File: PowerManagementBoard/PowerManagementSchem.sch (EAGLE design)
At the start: 112 parts, among them J1 D15S24A4GV00LF, J8 182-037-213R531, J9 182-025-213R531, U1 VX7805-500, U2 PYB20-Q24-S5, U3 PYB30-Q48-S5, U4 PYB30-Q48-S12, U5 3V3REG, U6 INA4180-SPLIT, U7 INA4180-SPLIT, U8 TEENSY-4.0SILK, U9 INA4180-SPLIT

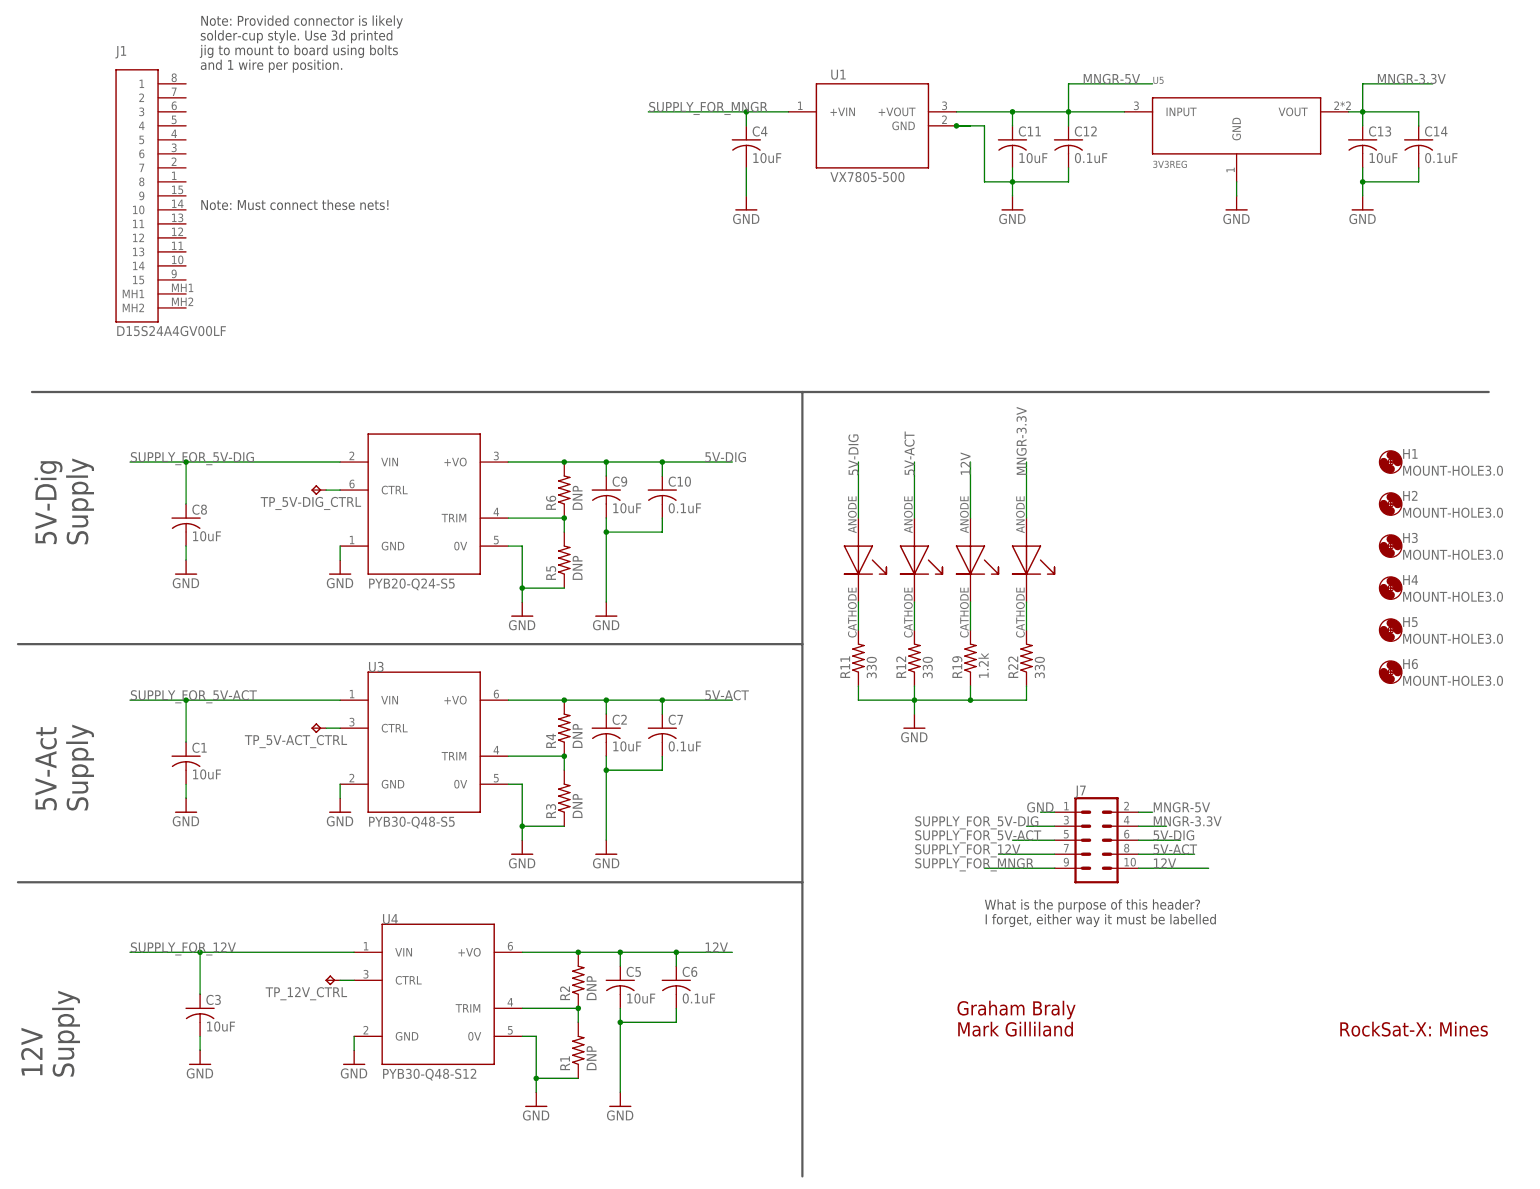
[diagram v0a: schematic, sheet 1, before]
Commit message: Moved components around on board. Updated power input header
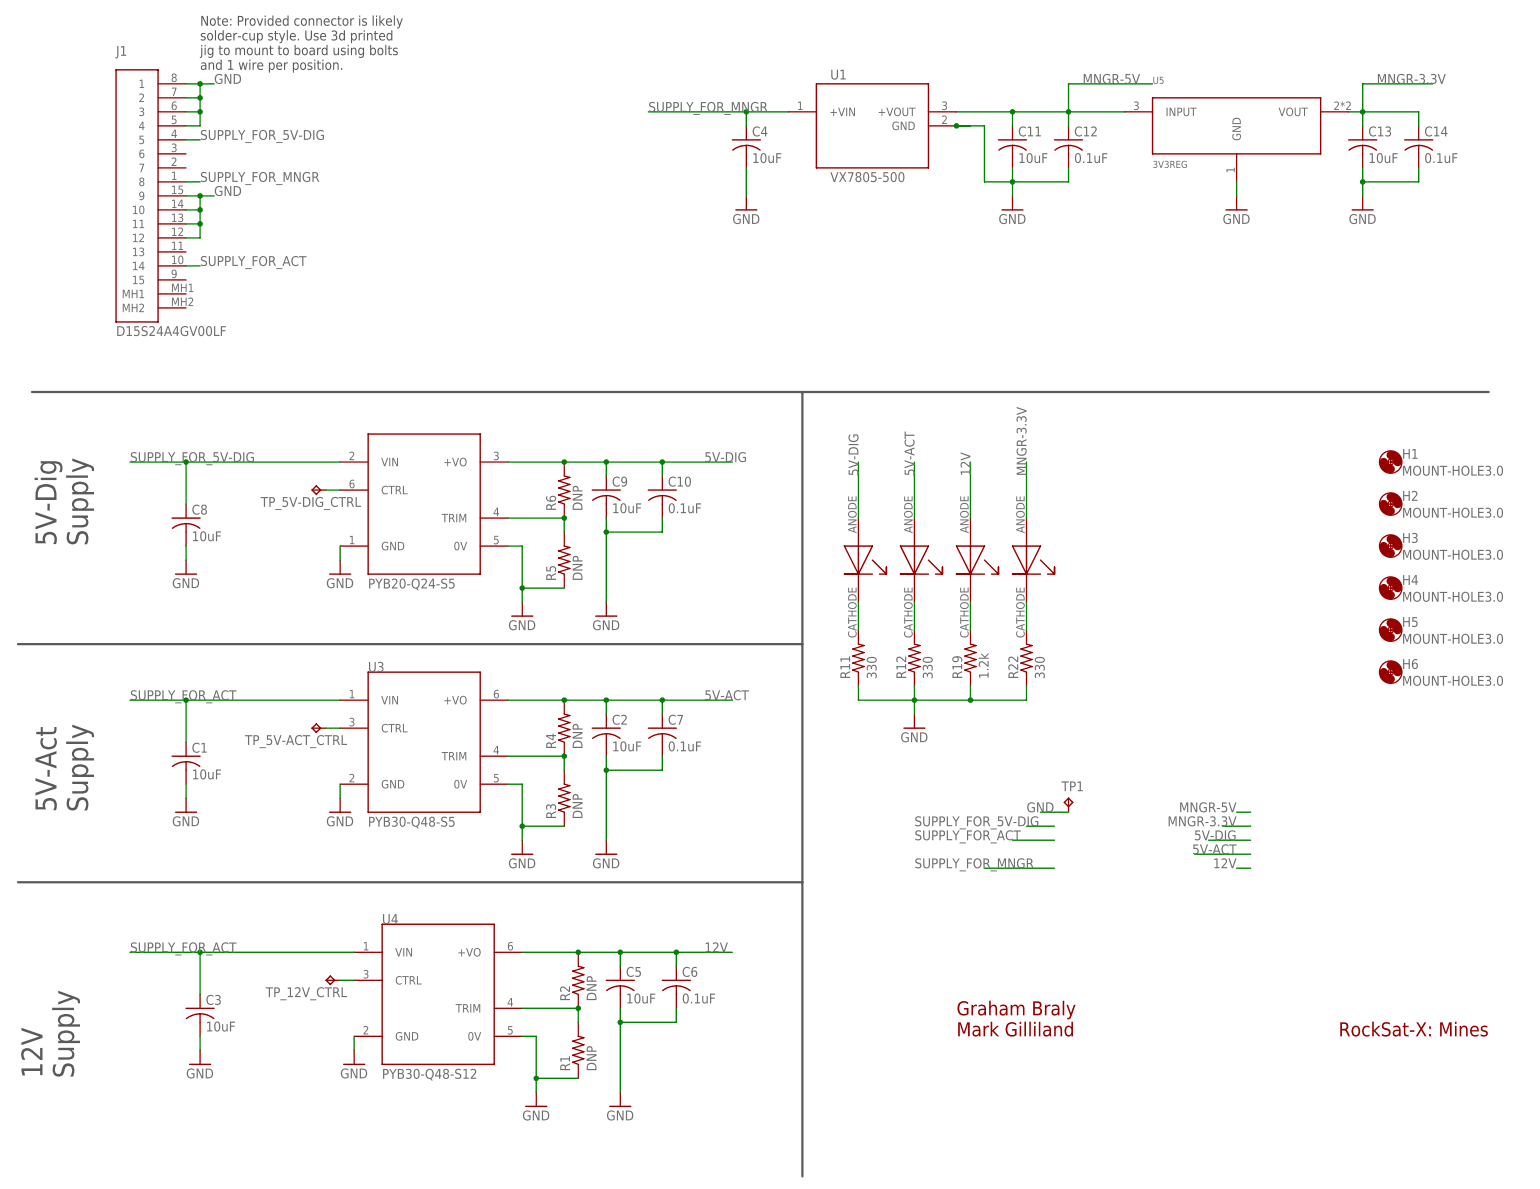
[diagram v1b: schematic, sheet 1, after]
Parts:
- removed J7: (no value), SparkFun-Connectors:CONN_05X2PTH
- added TP1: TPPAD1-13, testpad:TPPAD1-13
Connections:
- removed net SUPPLY_FOR_12V: C3.1, J7.7, U4.VIN
- removed net SUPPLY_FOR_5V-ACT: C1.1, J7.5, U3.VIN
- new net SUPPLY_FOR_ACT: C1.1, C3.1, J1.14, U3.VIN, U4.VIN
- net 12V: no longer J7.10
- net 5V-ACT: no longer J7.8
- net 5V-DIG: no longer J7.6
- net GND: now also J1.1, J1.10, J1.11, J1.12, J1.2, J1.3, J1.4, J1.9, TP1.TP; no longer J7.1
- net MNGR-3.3V: no longer J7.4
- net MNGR-5V: no longer J7.2
- net SUPPLY_FOR_5V-DIG: now also J1.5; no longer J7.3
- net SUPPLY_FOR_MNGR: now also J1.8; no longer J7.9
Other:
- note removed: "Note: Must connect these nets!"
- note removed: "What is the purpose of this header? I forget, either way it must be labelled"

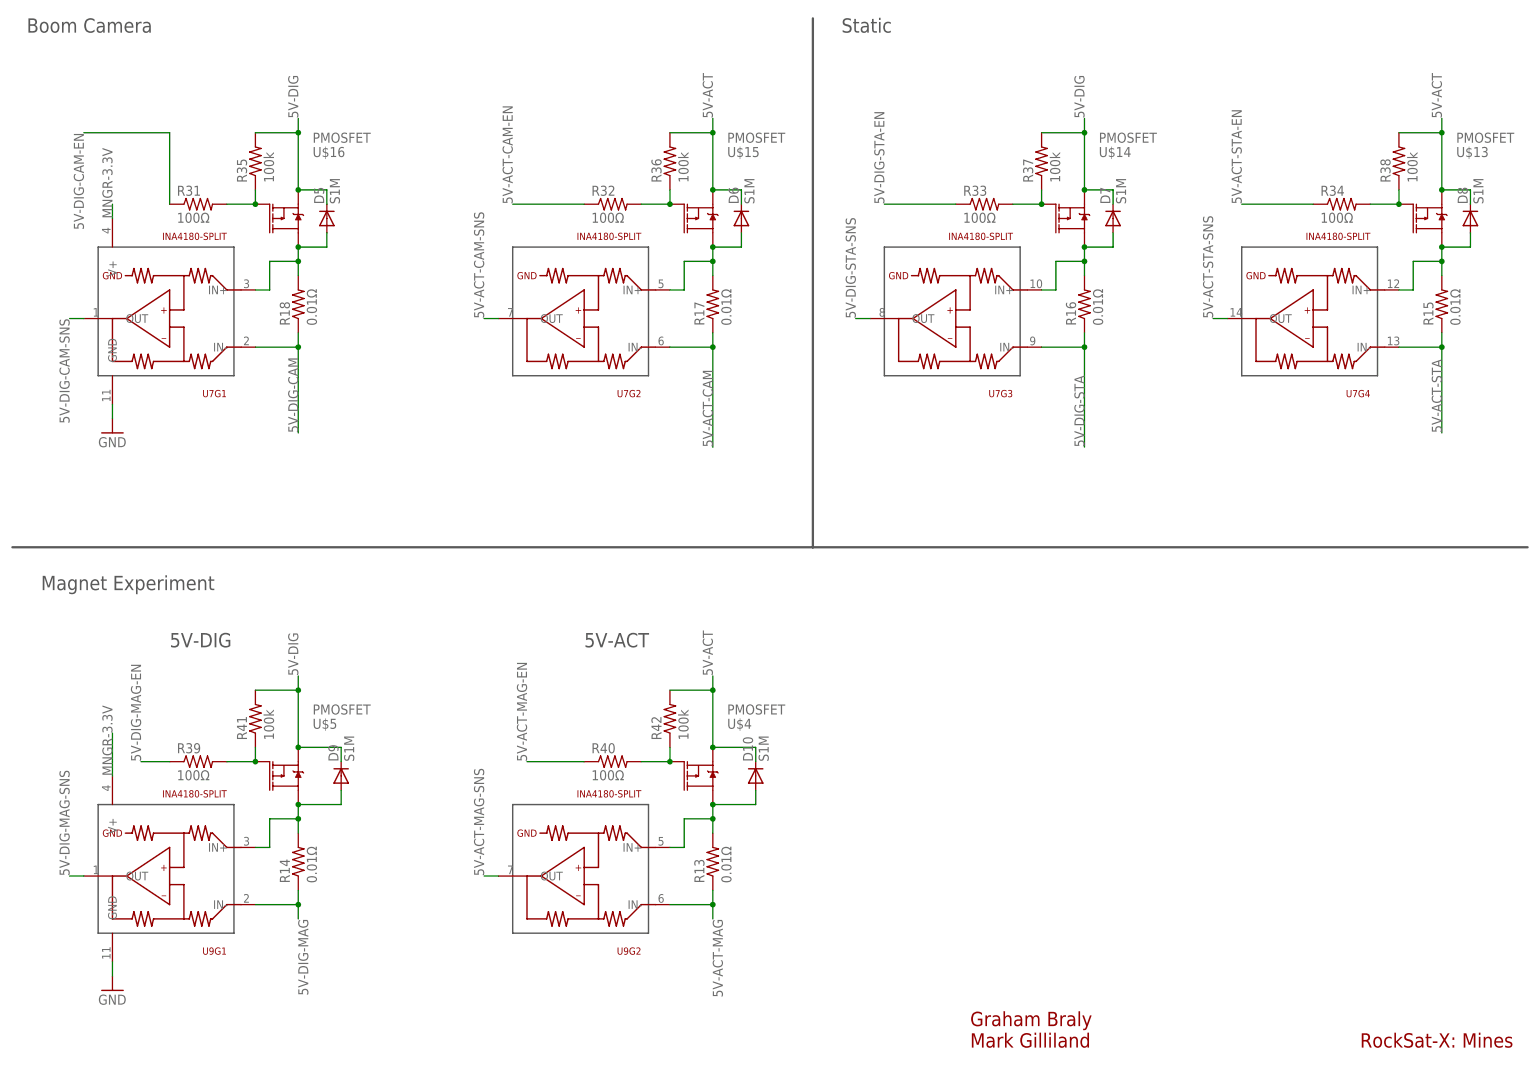
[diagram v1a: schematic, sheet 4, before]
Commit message: Rearranged MOSFET groups to assist with routing
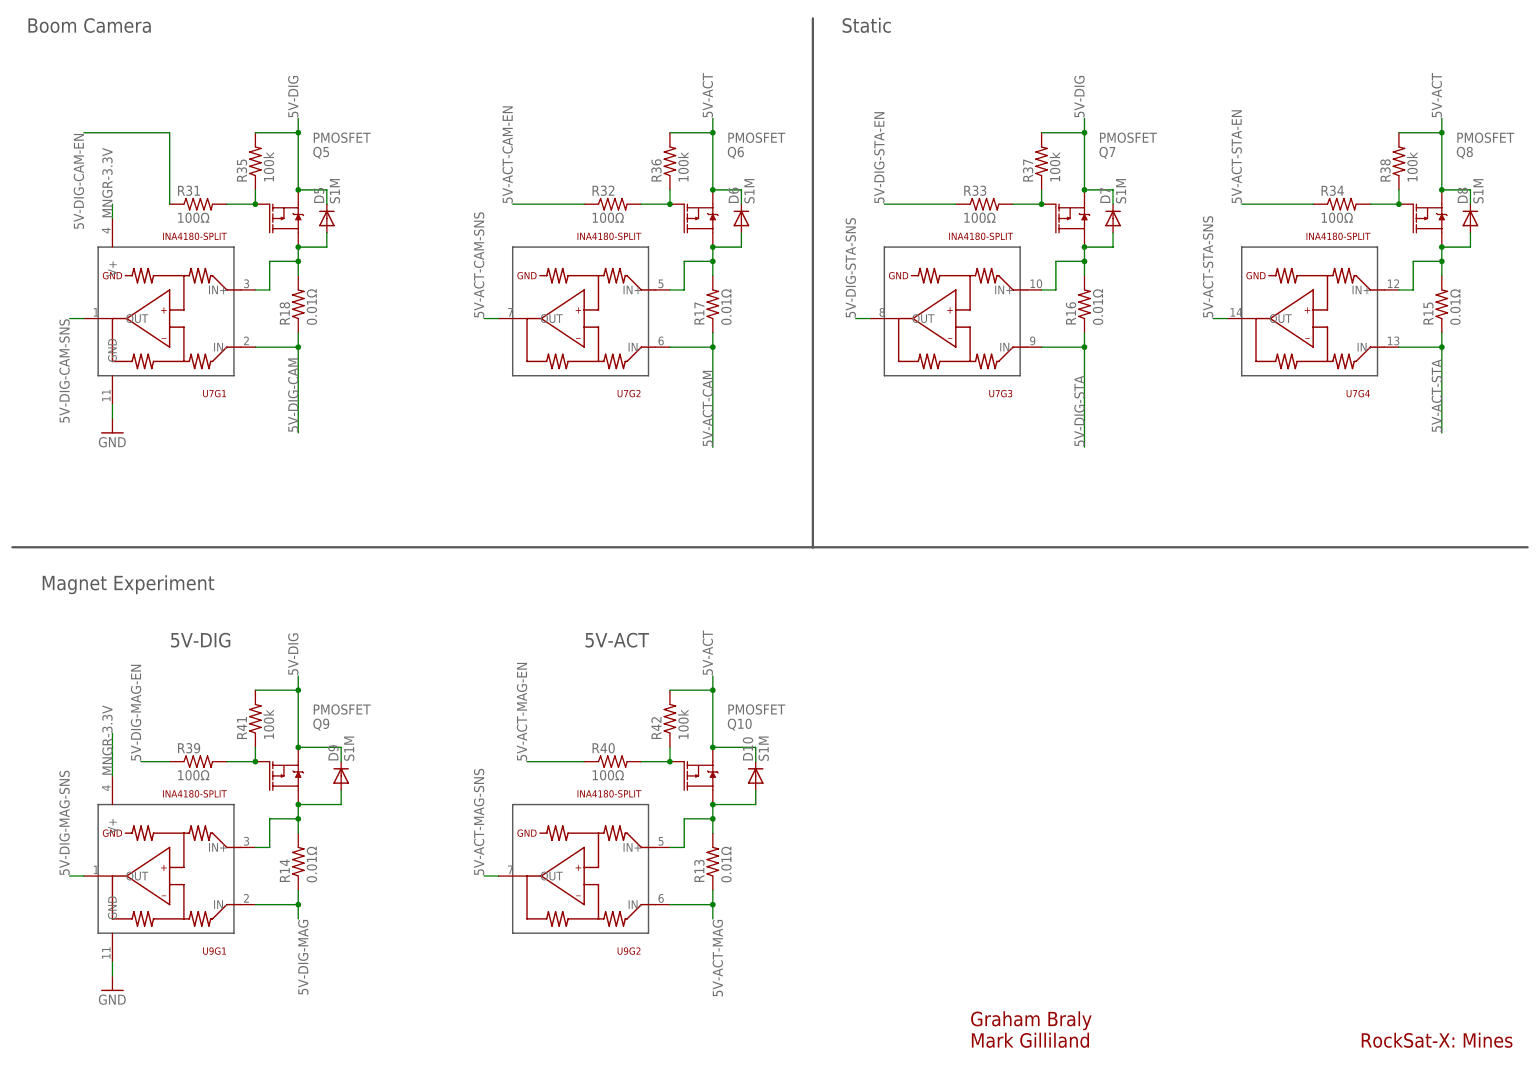
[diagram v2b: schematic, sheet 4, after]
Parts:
- renumbered U$1 to Q1, U$13 to Q8, U$14 to Q7, U$15 to Q6, U$16 to Q5, U$22 to Q11, U$23 to Q12, U$4 to Q10, U$5 to Q9, U$6 to Q2, U$7 to Q3, U$8 to Q4
